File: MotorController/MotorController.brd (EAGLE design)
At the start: 58.4 x 44.1 mm, 11 parts

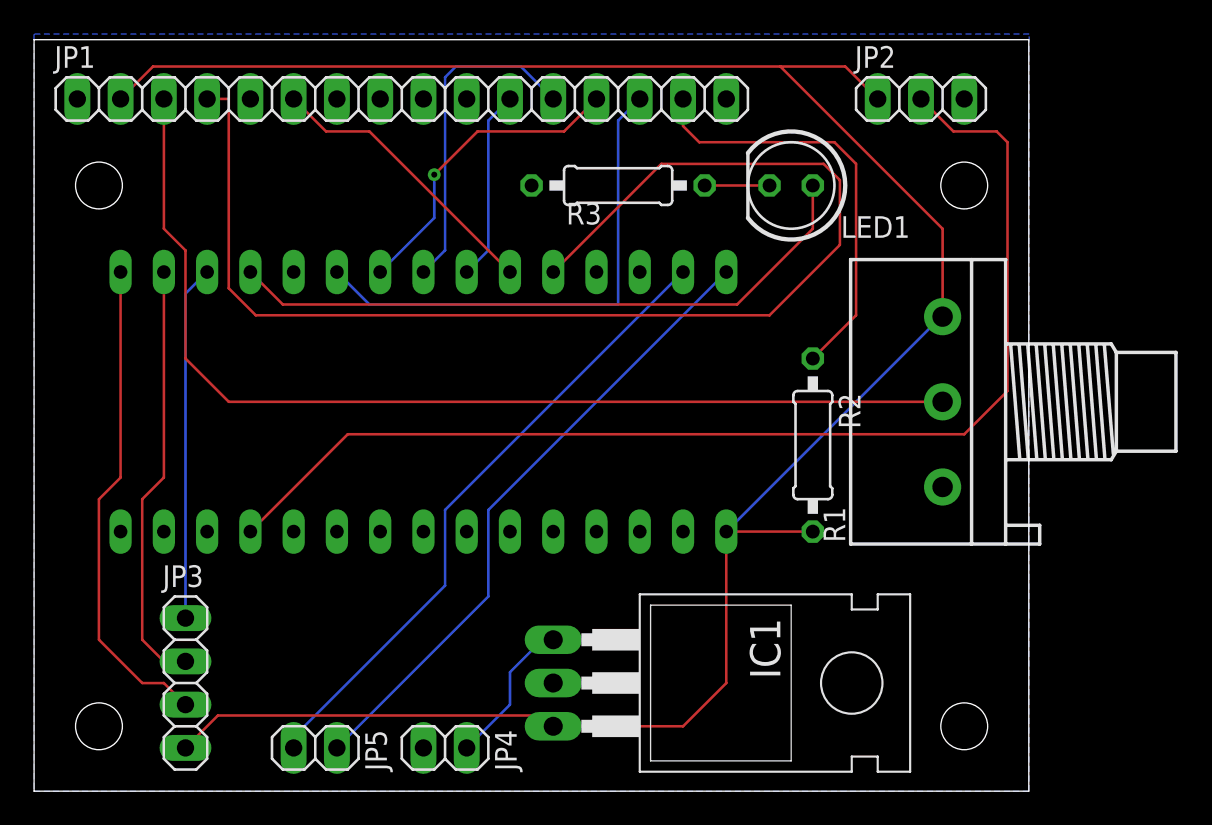
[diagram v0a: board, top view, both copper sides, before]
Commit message: Added button input
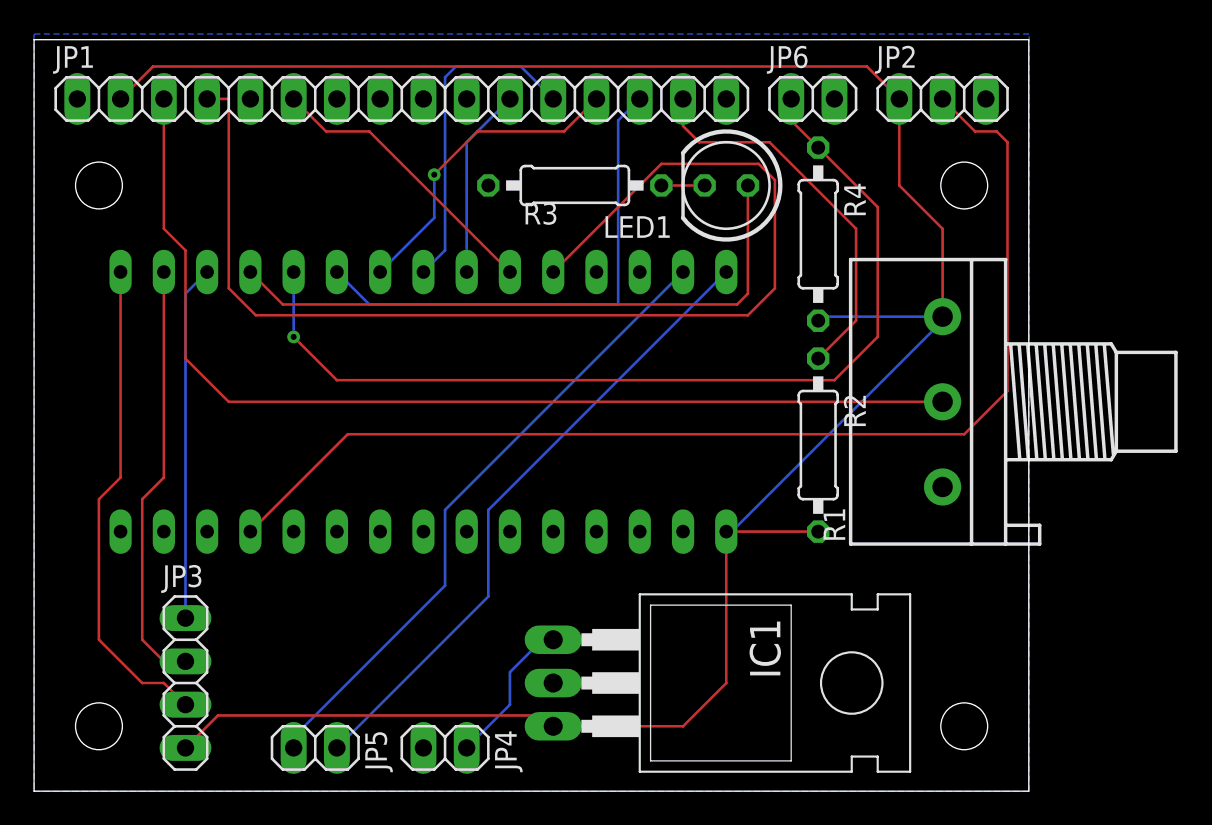
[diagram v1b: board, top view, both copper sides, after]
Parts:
- added JP6: (no value), GTOR - Connectors:1X02
- added R4: 10k, GTOR - Passive Components:1/4W-0.4
- moved LED1 3.81 mm to (40.6, 35.6)
- moved R3 2.54 mm to (31.8, 35.6)
- moved JP2 1.27 mm to (53.3, 40.6)
- moved R2 0.32 mm to (46.0, 20.3)
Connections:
- removed net N$4: U$1.D8
- new net BUTTON: JP6.1, R4.1, U$1.D8
- net 5V: now also R4.2
- net GND: now also JP6.2
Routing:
- net BUTTON: track 0.00 -> 56.3 mm, vias 0 -> 1
- net RS: track 74.3 -> 68.2 mm
- net 5V: track 130.5 -> 134.7 mm
- net A: track 25.2 -> 22.8 mm
- net LED: track 38.2 -> 36.6 mm
- net N$59: track 3.81 -> 2.54 mm
- net POT: track 68.6 -> 67.3 mm
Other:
- board text added: "BUTTON"
- board text removed: "220"
